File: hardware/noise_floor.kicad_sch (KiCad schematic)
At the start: 14 parts, among them J1 Input, J2 Output, J3 DC Power, J4 IO/Effect Connector 1 (IO Sid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, J5 IO/Effect Connector 2 (IO Sid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, J6 IO/Switch Connector 1 (IO Sid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, J7 IO/Switch Connector 2 (IO Sid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, J8 IO/Switch Connector 1 (Switch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, J9 IO/Switch Connector 2 (Switch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, SW1 Footswitch

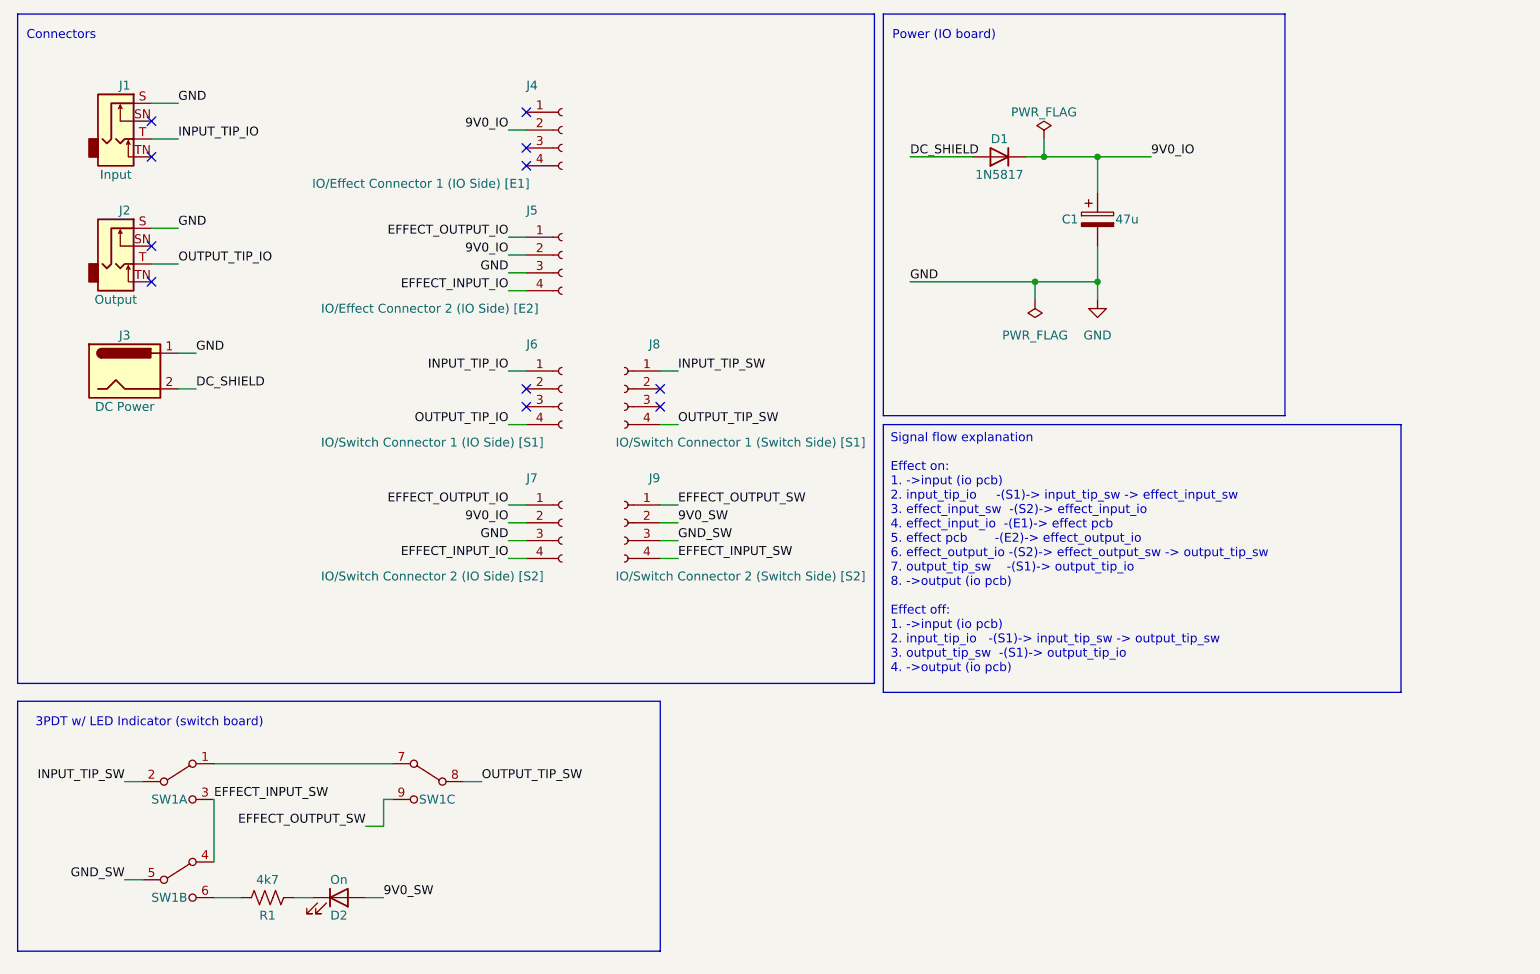
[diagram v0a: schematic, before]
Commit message: v0.03 updates:
 - switch to SMD resistor and diode to save space (particularly on footswitch board)
 - move IO and DC jacks to bottom of board and ensure they're on the correct side
 - consolidate to a single effect board connector.
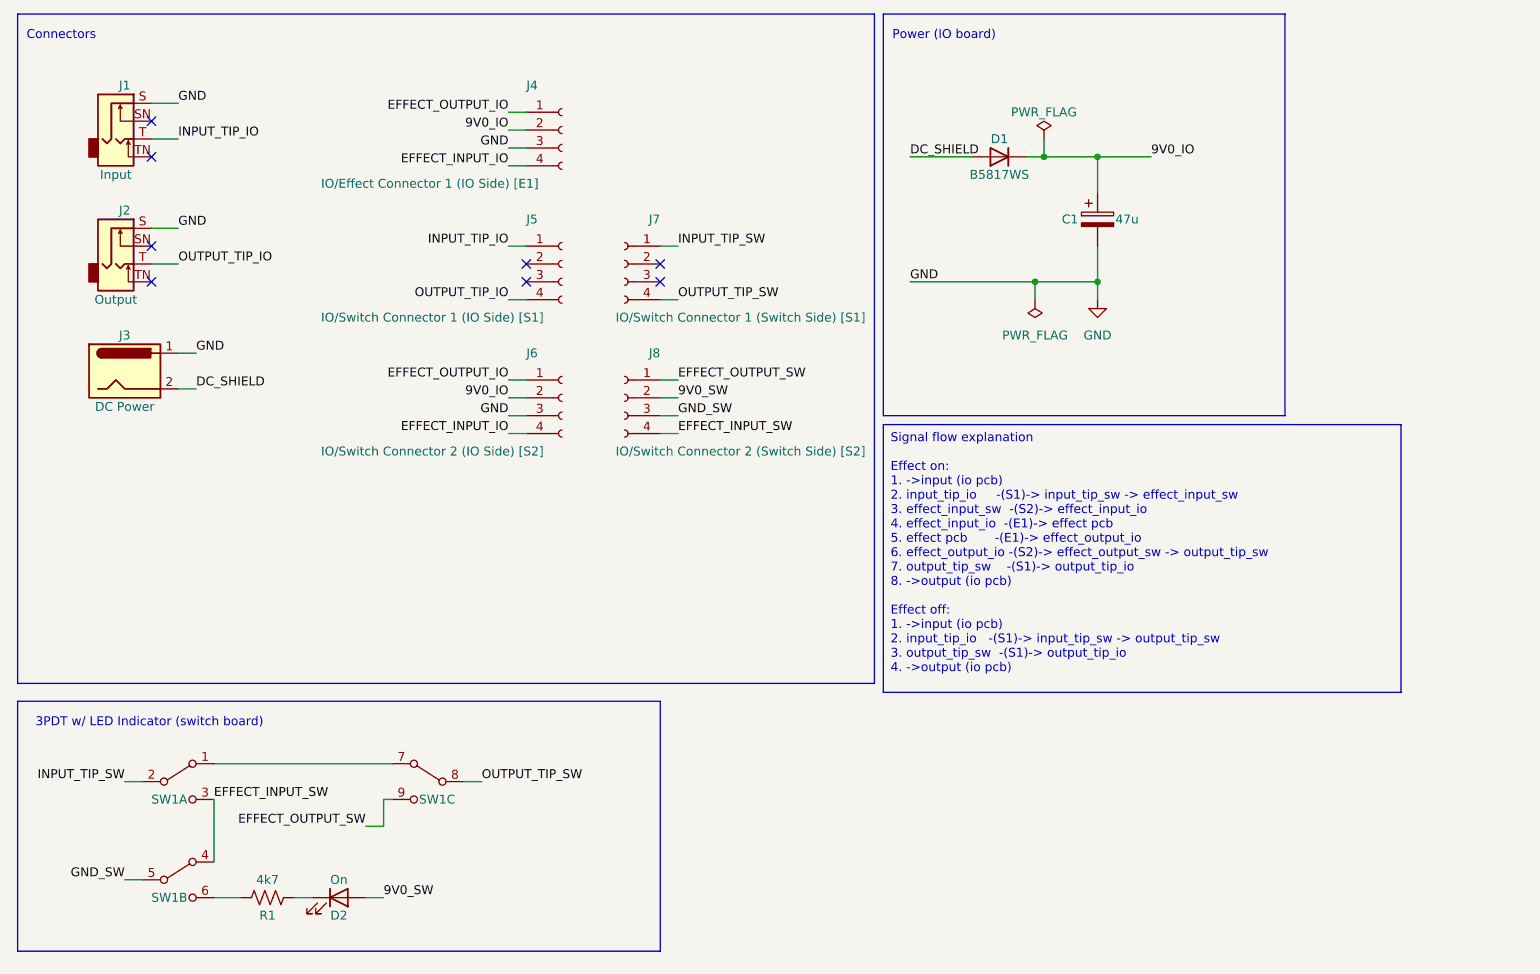
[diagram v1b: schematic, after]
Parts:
- removed J4: IO/Effect Connector 1 (IO Side) [E1], Connector_Molex:Molex_PicoBlade_53047-0410_1x04_P1.25mm_Vertical, symbol Connector:Conn_01x04_Socket
- D1: value 1N5817 -> B5817WS; footprint Diode_THT:D_DO-35_SOD27_P7.62mm_Horizontal -> Diode_SMD:D_SOD-323_HandSoldering
- J4: renamed from J5; value IO/Effect Connector 2 (IO Side) [E2] -> IO/Effect Connector 1 (IO Side) [E1]
- R1: footprint Resistor_THT:R_Axial_DIN0207_L6.3mm_D2.5mm_P7.62mm_Horizontal -> Resistor_SMD:R_1206_3216Metric_Pad1.30x1.75mm_HandSolder
- renumbered J6 to J5, J7 to J6, J8 to J7, J9 to J8
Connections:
- no-connect marks 11 -> 8
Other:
- moved on the sheet: J4, J5, J6, J7, J8

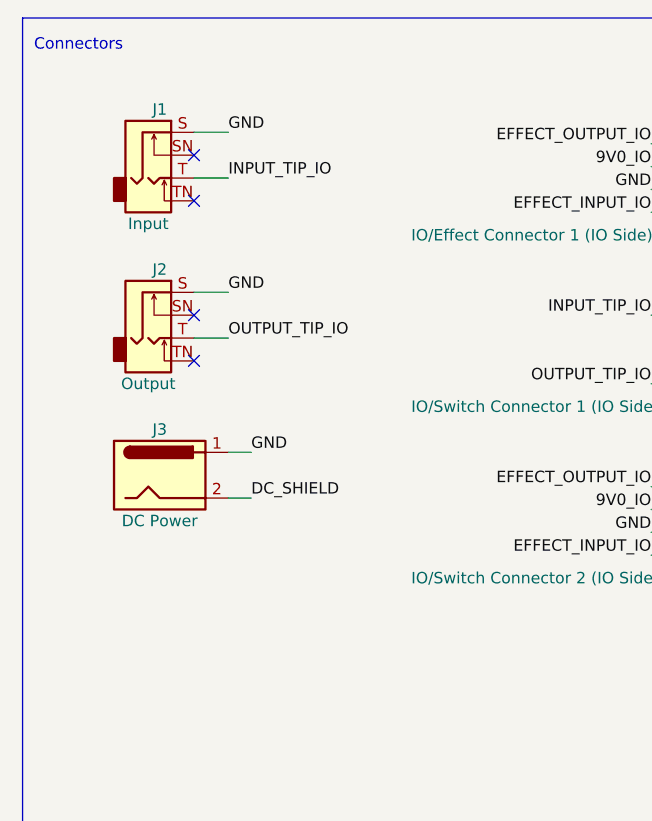
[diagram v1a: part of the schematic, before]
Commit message: Some updates based on feedback from freestompboxes.org folks:
 - Add back thermal reliefs on ground pads
 - Switch to stereo jacks for improved mechanical support
 - Use switched symbol/footprint for DC Barrel jack, correct circuit to suit (still need to add switching on input jack)
 - Add 3D models for various parts (courtesy of Vasily Kashirin - https://grabcad.com/vasily.kashirin-1/models?page=1)
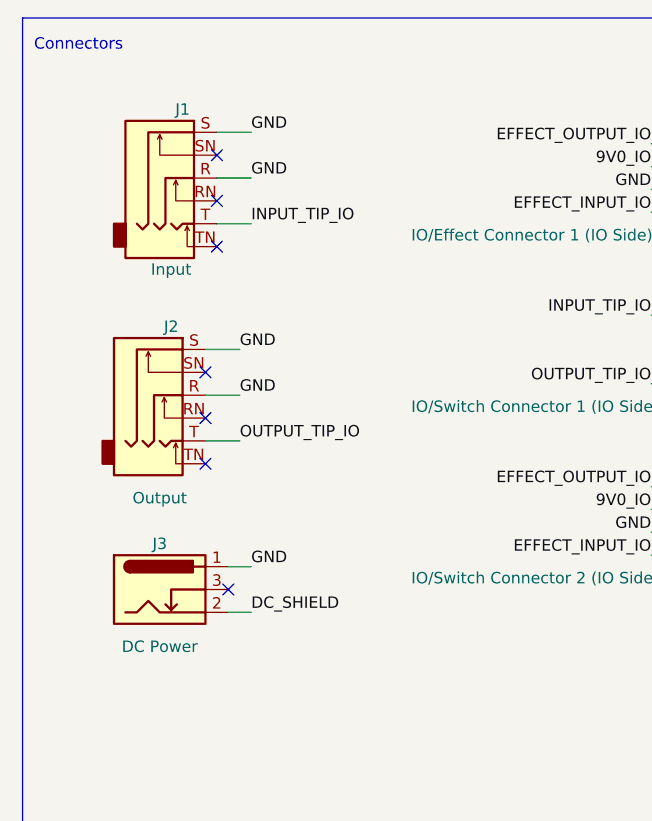
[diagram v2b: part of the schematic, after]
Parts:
- J1, J2: footprint Connector_Audio:Jack_6.35mm_Neutrik_NMJ4HCD2_Horizontal -> noise_floor:Jack_6.35mm_Neutrik_NMJ6HCD2_Horizontal-3DModel_from_Vasily_Kashirin; symbol Connector_Audio:AudioJack2_Switch -> Connector_Audio:AudioJack3_Switch
- J3: footprint Connector_BarrelJack:BarrelJack_GCT_DCJ200-10-A_Horizontal -> noise_floor:BarrelJack_GCT_DCJ200-10-A_Horizontal_with_3DModel_from_Vasily_Kashirin; symbol Connector:Barrel_Jack -> Connector:Barrel_Jack_Switch
- J4, J5, J6, J7, J8: footprint Connector_Molex:Molex_PicoBlade_53047-0410_1x04_P1.25mm_Vertical -> noise_floor:Molex_PicoBlade_53047-0410_1x04_P1.25mm_Vertical_with_3D_Model
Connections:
- net GND: now also J1.R, J2.R
- no-connect marks 8 -> 11

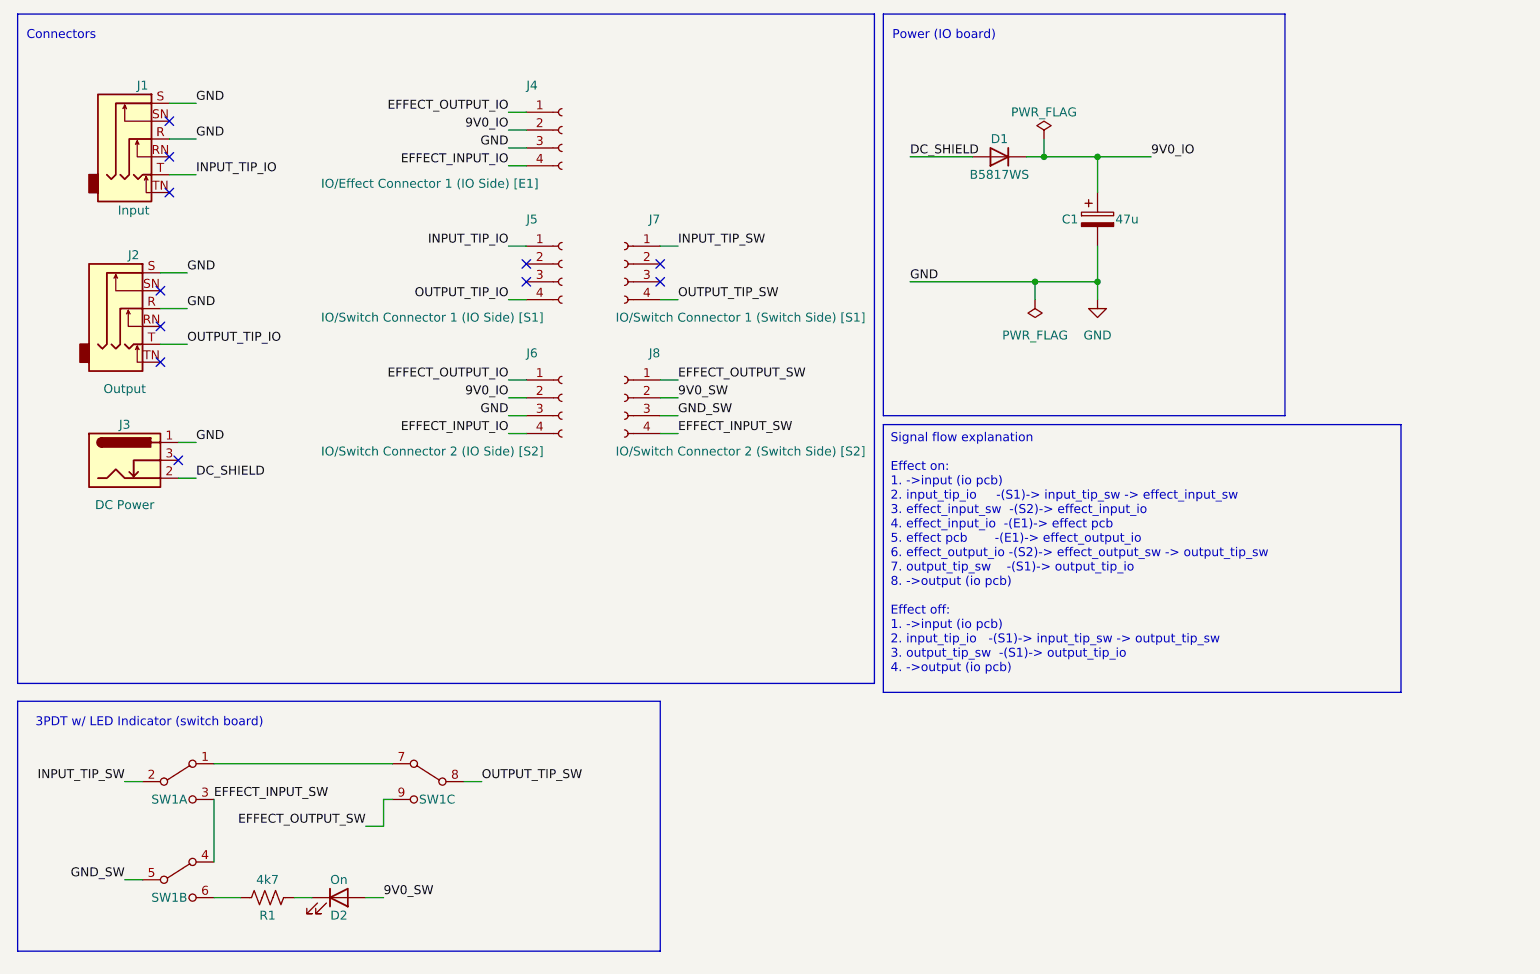
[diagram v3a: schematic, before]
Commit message: v0.05, added switched power input and optional battery connection
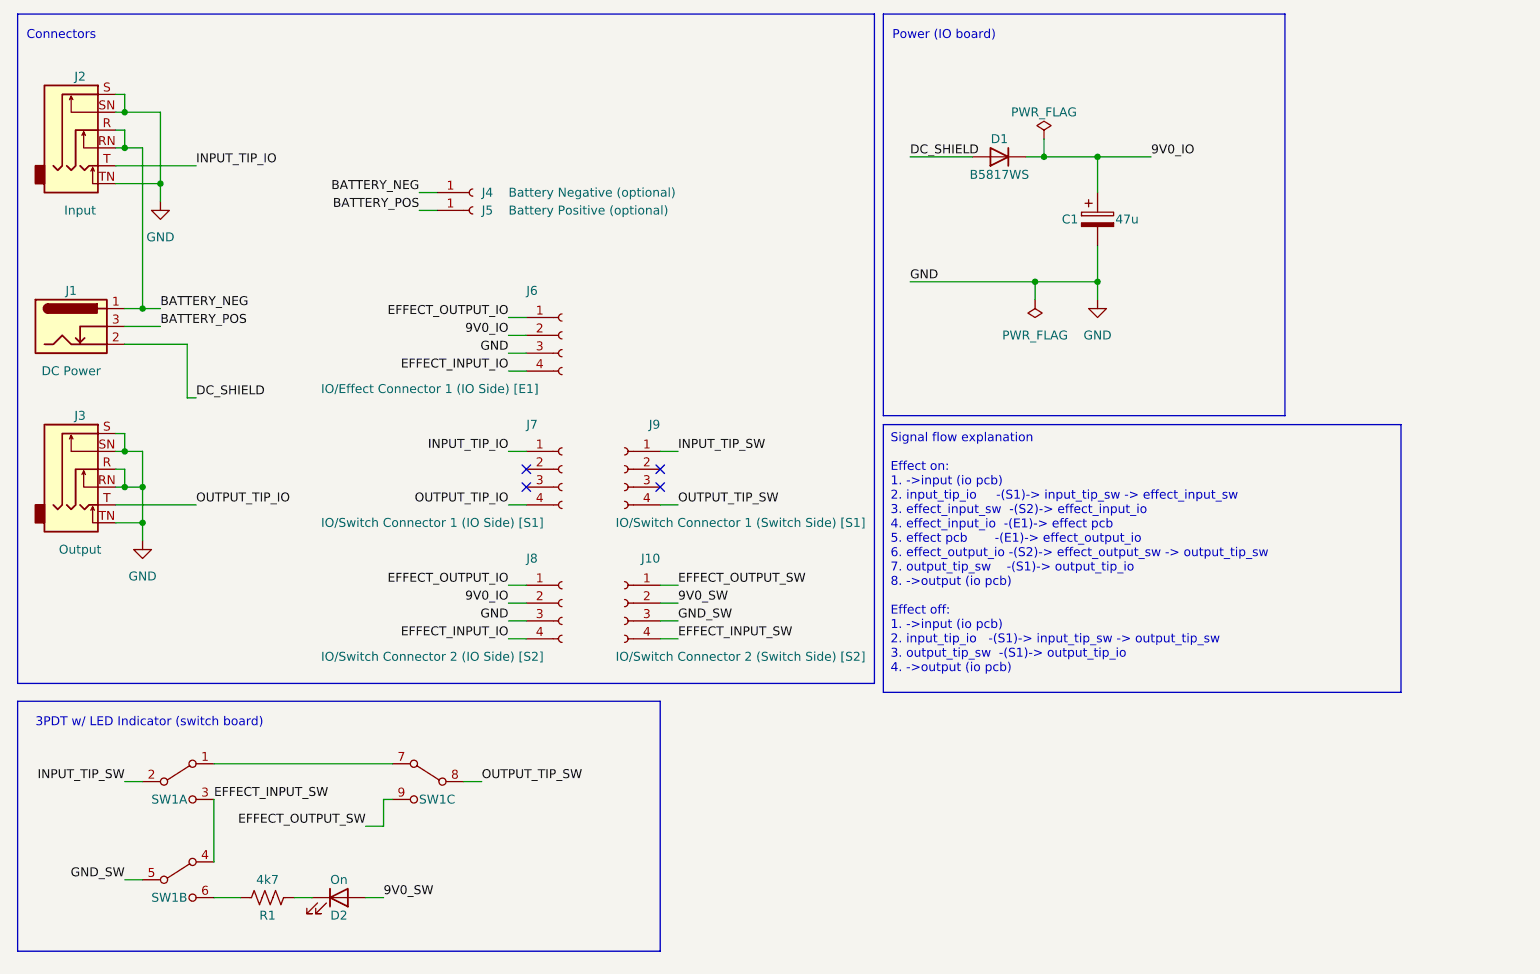
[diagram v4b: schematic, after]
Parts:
- added J4: Battery Negative (optional), Connector_Wire:SolderWire-0.25sqmm_1x01_D0.65mm_OD2mm, symbol Connector:Conn_01x01_Socket
- added J5: Battery Positive (optional), Connector_Wire:SolderWire-0.25sqmm_1x01_D0.65mm_OD2mm, symbol Connector:Conn_01x01_Socket
- renumbered J3 to J1, J8 to J10, J1 to J2, J2 to J3, J4 to J6, J5 to J7, J6 to J8, J7 to J9
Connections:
- net GND: now also J2.SN, J2.TN, J3.RN, J3.SN, J3.TN; no longer J1.1, J2.R
- net BATTERY_POS: now reaches J1.3
- net BATTERY_POS: now also J5.1 (Pin_1)
- net BATTERY_NEG: now reaches J2.RN
- net BATTERY_NEG: now also J1.1, J2.R, J4.1 (Pin_1)
- no-connect marks 11 -> 4
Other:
- moved on the sheet: J1, J10, J2, J3, J6, J7, J8, J9

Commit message: Remove ground from output switch line, fix ground split ground plane
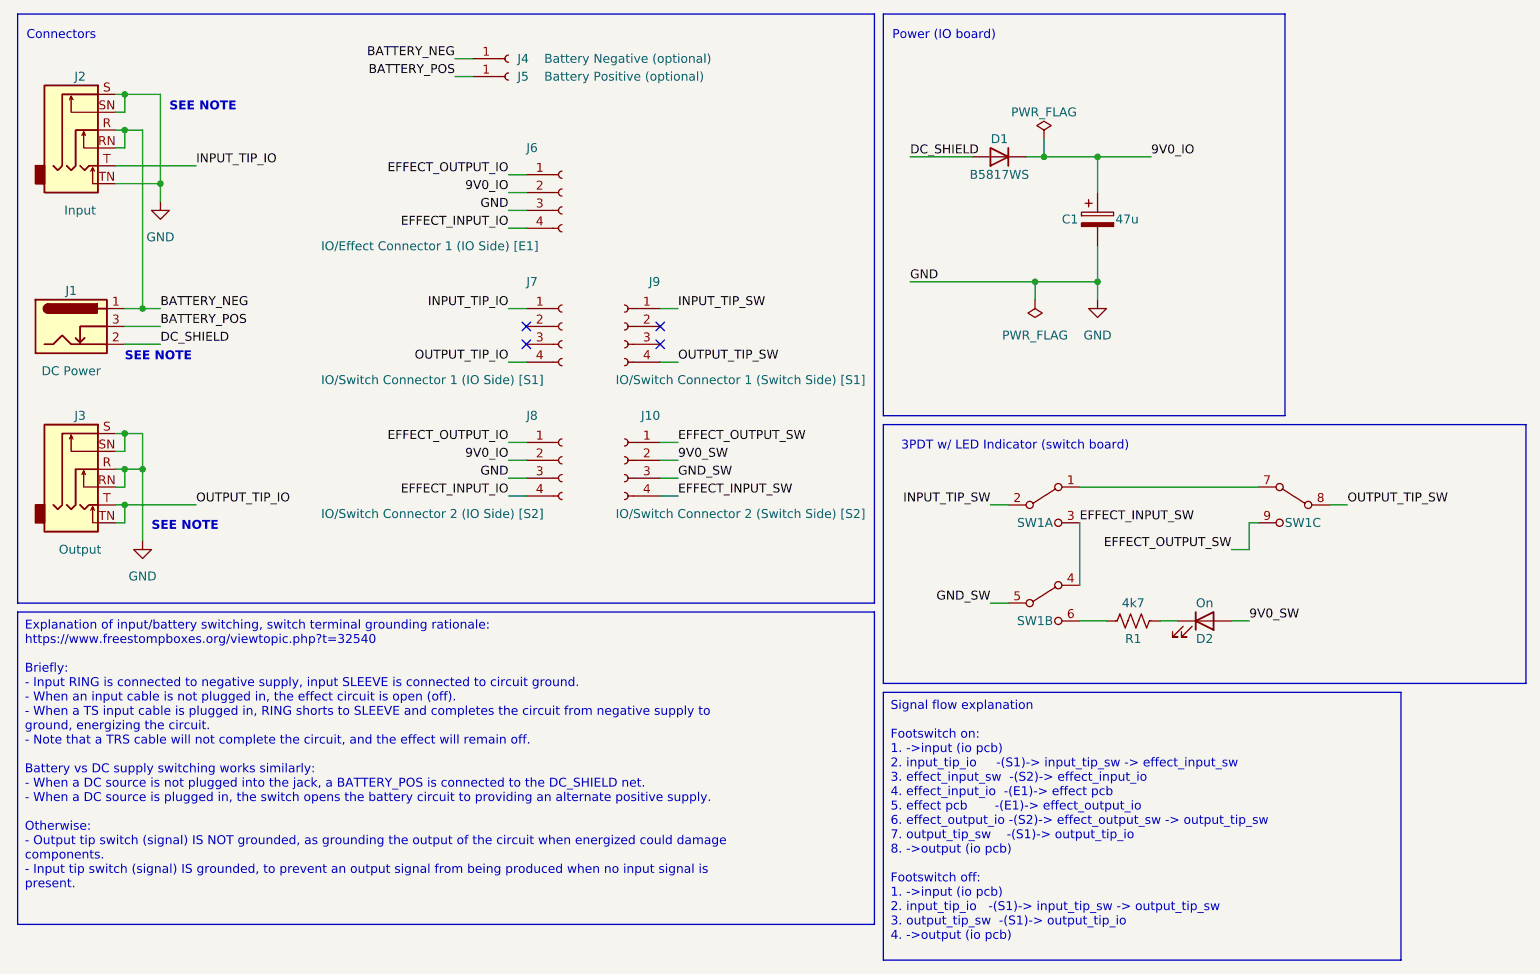
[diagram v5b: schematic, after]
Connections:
- net GND: no longer J3.TN
- net OUTPUT_TIP_IO: now also J3.TN
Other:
- note added: "SEE NOTE"
- moved on the sheet: D2, J10, J4, J5, J6, J7, J8, J9, R1, SW1A, SW1B, SW1C
